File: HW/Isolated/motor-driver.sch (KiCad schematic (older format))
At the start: 30 parts

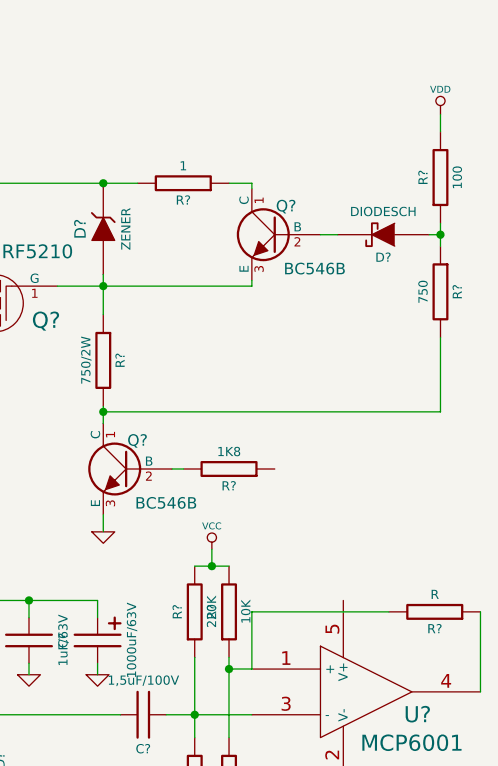
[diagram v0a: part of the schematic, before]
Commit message: Schematic modified
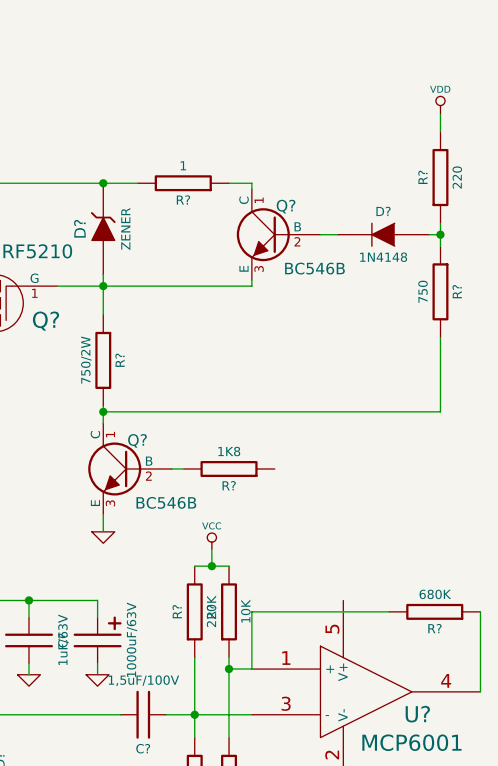
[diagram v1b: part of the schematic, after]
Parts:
- removed D?: DIODESCH, symbol DIODESCH
- added D?: 1N4148, D2, symbol DIODE
- R?: value R -> 680K; footprint ~ -> R4
- R?: value 100 -> 220
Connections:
- net at Q?.2 (B): now also D?.2 (K)
- net at R?.2, R?.2: now also D?.1 (A)
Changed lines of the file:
@@
 P 3400 5150
 F 0 "R?" H 3400 5075 40  0000 C CNN
-F 1 "R" H 3400 5225 40  0000 C CNN
-F 2 "~" H 3400 5150 60  0000 C CNN
+F 1 "680K" H 3400 5225 40  0000 C CNN
+F 2 "R4" H 3400 5150 60  0001 C CNN
 F 3 "~" H 3400 5150 60  0000 C CNN
 	1    3400 5150
@@
 P 3425 3250
 F 0 "R?" H 3425 3175 40  0000 C CNN
-F 1 "100" H 3425 3325 40  0000 C CNN
+F 1 "220" H 3425 3325 40  0000 C CNN
 F 2 "R4" H 3425 3250 60  0001 C CNN
 F 3 "~" H 3425 3250 60  0000 C CNN
@@
 Wire Wire Line
 	3425 2975 3425 3050
-$Comp
-L DIODESCH D?
-U 1 1 54C35AF0
+Wire Wire Line
+	2900 3500 2975 3500
+Wire Wire Line
+	3425 3450 3425 3550
+Wire Wire Line
+	3375 3500 3425 3500
+Connection ~ 3425 3500
+Wire Wire Line
+	1950 4275 3425 4275
+Wire Wire Line
+	3425 4275 3425 3950
+Connection ~ 1950 4275
+$Comp
+L DIODE D?
+U 1 1 54C42B48
 P 3175 3500
 F 0 "D?" H 3175 3600 40  0000 C CNN
-F 1 "DIODESCH" H 3175 3400 40  0000 C CNN
-F 2 "" H 3175 3500 60  0000 C CNN
+F 1 "1N4148" H 3175 3400 40  0000 C CNN
+F 2 "D2" H 3175 3500 60  0001 C CNN
 F 3 "" H 3175 3500 60  0000 C CNN
 	1    3175 3500
-	-1   0    0    1
-$EndComp
-Wire Wire Line
-	2900 3500 2975 3500
-Wire Wire Line
-	3425 3450 3425 3550
-Wire Wire Line
-	3375 3500 3425 3500
-Connection ~ 3425 3500
-Wire Wire Line
-	1950 4275 3425 4275
-Wire Wire Line
-	3425 4275 3425 3950
-Connection ~ 1950 4275
+	-1   0    0    -1
+$EndComp
 $EndSCHEMATC
